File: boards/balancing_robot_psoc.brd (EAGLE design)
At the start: 35 x 75 mm, 19 parts

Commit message: PsoC and MPU board finished
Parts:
- removed C1, C2, C5, C6: 100n, rcl:C0603
- removed C10, C12: 3n3, rcl:C0603
- removed C3, C4, C7, C8: 10u, rcl:153CLV-0405
- removed JP2, JP3: (no value), pinhead:1X06
- removed U$3, U$6: TB6612FNG, SparkFun-PowerIC:SSOP24
- removed U$4: TRANSFORMER, DC_DC_transformer:TRANSFORMER
- removed X1: (no value), con-ptr500:AK500/2
- added LED2, LED3, LED4, LED5, LED6, LED7, LED8: (no value), led:CHIP-LED0603
- added R10, R11, R12, R13, R14, R15, R16, R17, R2, R3, R4, R5, R6, R7, R8, R9: (no value), rcl:R0603
- added U$1: PSOC/PROC, SmartCart:PSOC/PROC_SOCKET
- added U$5: MPU, MPU:MPU
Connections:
- removed net OUT_MOTOR1_1: C12.2, JP2.6, U$6.1, U$6.11, U$6.12, U$6.2
- removed net OUT_MOTOR1_2: C12.1, JP2.5, U$6.5, U$6.6, U$6.7, U$6.8
- removed net OUT_MOTOR2_1: C10.2, JP3.6, U$3.1, U$3.11, U$3.12, U$3.2
- removed net OUT_MOTOR2_2: C10.1, JP3.5, U$3.5, U$3.6, U$3.7, U$3.8
- new net 3V3: JP1.7, JP1.8, R7.2
- new net 5V: JP1.1, JP1.2, R1.2, R6.2, U$5.P$1
- new net ADC_BAT: R8.2, R9.1, U$1.1.16
- new net CONN1: R10.2, R11.2, R12.2, R13.2, R14.2, R15.2, R16.2, R17.1
- new net GPIO_0: JP1.11, U$1.1.7
- new net GPIO_1: JP1.12, U$1.1.9
- new net I2C_SCL: JP1.14, U$1.1.19, U$5.P$3
- new net I2C_SDA: JP1.13, U$1.1.20, U$5.P$4
- new net LED0: LED4.C, U$1.2.19
- new net LED1: LED5.C, U$1.2.20
- new net LED2: LED3.C, U$1.2.17
- new net LED3: LED6.C, U$1.2.18
- new net LED4: LED2.C, U$1.2.15
- new net LED5: LED7.C, U$1.2.16
- new net LED6: LED8.C, U$1.2.14
- new net N$1: R2.2, U$1.1.23
- new net N$11: LED4.A, R12.1
- new net N$12: LED5.A, R13.1
- new net N$13: LED6.A, R14.1
- new net N$14: LED7.A, R15.1
- new net N$15: LED8.A, R16.1
- new net N$2: R5.1, U$1.2.13
- new net N$3: R3.2, U$1.2.2
- new net N$4: R4.1, U$1.1.2
- new net N$5: LED2.A, R10.1
- new net N$6: LED3.A, R11.1
- new net POWER_SUP: R17.2, R2.1, R3.1, R4.2, R5.2, R6.1, R7.1
- new net UART_RX: JP1.10, U$1.2.5
- new net UART_TX: JP1.9, U$1.2.9
- net ENK_MOTOR1A: now also U$1.1.22; no longer JP2.3
- net ENK_MOTOR1B: now also U$1.1.21; no longer JP2.2
- net ENK_MOTOR2A: now also U$1.1.18; no longer JP3.3
- net ENK_MOTOR2B: now also U$1.1.17; no longer JP3.2
- net GND: now also R8.1, U$1.1.1, U$1.1.24, U$1.2.4, U$5.P$2; no longer C1.1, C2.2, C3.-, C4.-, C5.1, C6.2, C7.-, C8.-, JP2.1, JP3.1, U$3.10, U$3.18, U$3.3, U$3.4, U$3.9, U$4.1IN-, U$4.1OUT-, U$4.2IN-, U$4.2OUT-, U$6.10, U$6.18, U$6.3, U$6.4, U$6.9, X1.2
- net MOTOR1_1: now also U$1.2.3; no longer U$6.17, U$6.21
- net MOTOR1_2: now also U$1.2.7; no longer U$6.16, U$6.22
- net MOTOR1_PWM: now also U$1.2.8; no longer U$6.15, U$6.23
- net MOTOR2_1: now also U$1.2.10; no longer U$3.17, U$3.21
- net MOTOR2_2: now also U$1.2.11; no longer U$3.16, U$3.22
- net MOTOR2_PWM: now also U$1.2.12; no longer U$3.15, U$3.23
- net VCC: now also R9.2; no longer C1.2, C2.1, C3.+, C4.+, C5.2, C6.1, C7.+, C8.+, JP1.1, JP1.2, JP2.4, JP3.4, R1.2, U$3.13, U$3.14, U$3.20, U$3.24, U$4.1IN+, U$4.1OUT+, U$4.2IN+, U$4.2OUT+, U$6.13, U$6.14, U$6.20, U$6.24, X1.1
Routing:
- net VCC: track 253.0 -> 5.74 mm, vias 7 -> 0
- net POWER_SUP: track 0.00 -> 121.8 mm, vias 0 -> 2
- net I2C_SCL: track 0.00 -> 60.6 mm
- net I2C_SDA: track 0.00 -> 60.1 mm
- net OUT_MOTOR2_1: track 57.5 -> 0.00 mm, vias 4 -> 0
- net OUT_MOTOR2_2: track 39.4 -> 0.00 mm, vias 2 -> 0
- net 5V: track 0.00 -> 37.9 mm
- net UART_TX: track 0.00 -> 35.8 mm, vias 0 -> 1
- net ADC_BAT: track 0.00 -> 32.0 mm
- net LED4: track 0.00 -> 31.5 mm
- net OUT_MOTOR1_1: track 29.5 -> 0.00 mm, vias 4 -> 0
- net UART_RX: track 0.00 -> 28.8 mm, vias 0 -> 1
- net LED2: track 0.00 -> 26.1 mm
- net CONN1: track 0.00 -> 22.8 mm
- net LED6: track 0.00 -> 21.9 mm
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
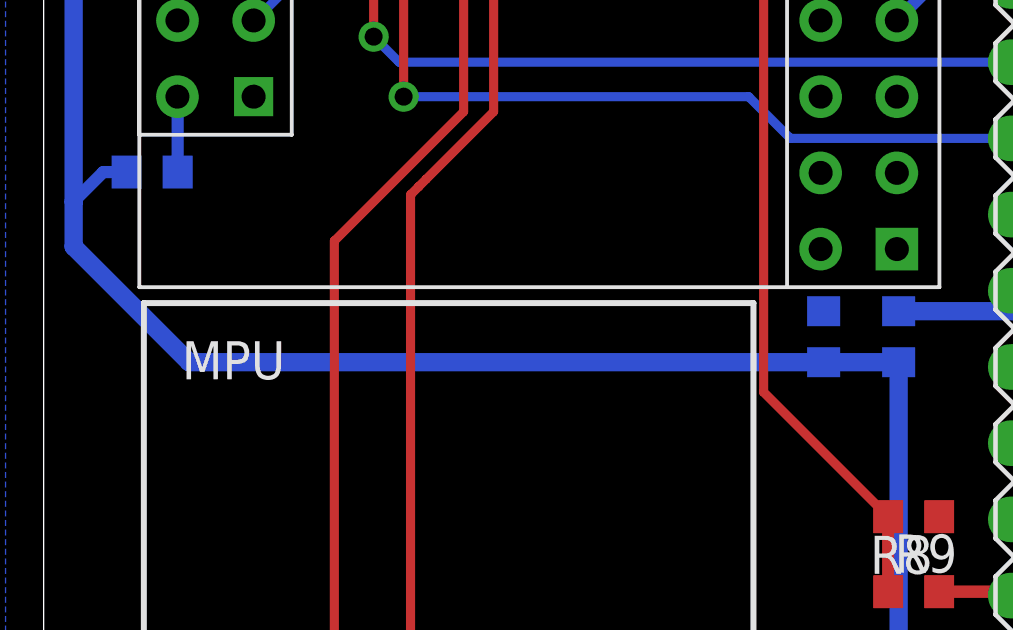
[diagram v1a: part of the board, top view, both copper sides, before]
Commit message: added capacitors on power sup line on psoc board
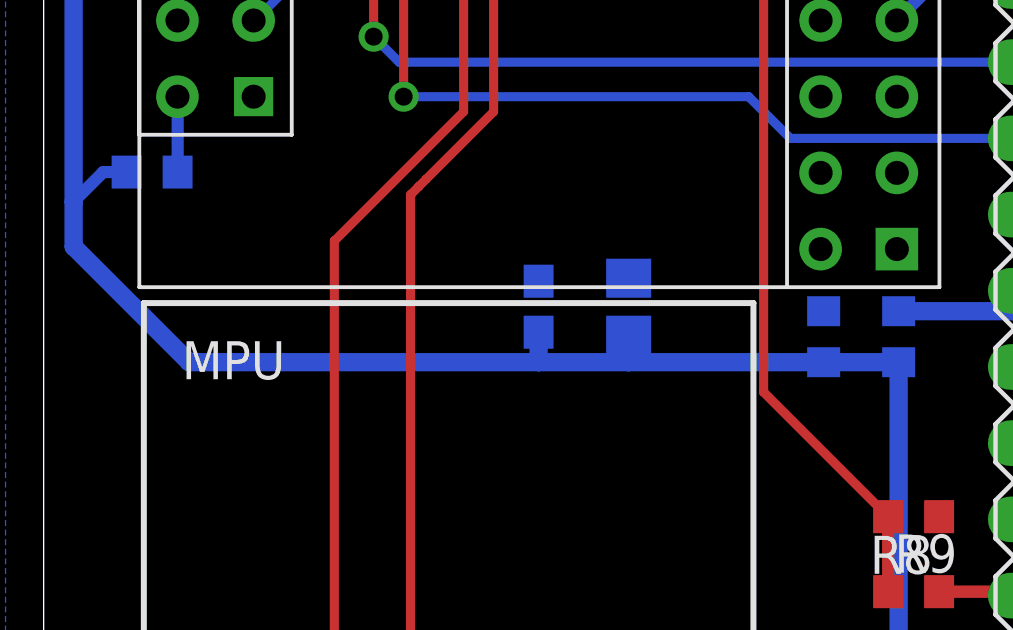
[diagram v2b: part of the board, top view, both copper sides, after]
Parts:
- added C1: (no value), rcl:C0603
- added C2: (no value), rcl:C0805
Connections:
- net GND: now also C1.2, C2.2
- net POWER_SUP: now also C1.1, C2.1
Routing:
- net POWER_SUP: track 121.8 -> 123.7 mm
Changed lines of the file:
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@@
 <layer number="27" name="tValues" color="7" fill="1" visible="yes" active="yes"/>
 <layer number="28" name="bValues" color="7" fill="1" visible="yes" active="yes"/>
-<layer number="29" name="tStop" color="7" fill="3" visible="yes" active="yes"/>
-<layer number="30" name="bStop" color="7" fill="6" visible="yes" active="yes"/>
+<layer number="29" name="tStop" color="7" fill="3" visible="no" active="yes"/>
+<layer number="30" name="bStop" color="7" fill="6" visible="no" active="yes"/>
 <layer number="31" name="tCream" color="7" fill="4" visible="no" active="yes"/>
 <layer number="32" name="bCream" color="7" fill="5" visible="no" active="yes"/>
@@
 <element name="R16" library="rcl" package="R0603" value="" x="7" y="66" rot="R90"/>
 <element name="R17" library="rcl" package="R0603" value="" x="17.5" y="69.5" rot="R90"/>
+<element name="C1" library="rcl" package="C0603" value="" x="16.5" y="23" rot="MR90"/>
+<element name="C2" library="rcl" package="C0805" value="" x="19.5" y="23" rot="MR90"/>
 </elements>
 <signals>
@@
 <via x="10.16" y="50.8" extent="1-16" drill="0.6"/>
 <via x="21.59" y="5.08" extent="1-16" drill="0.6"/>
+<contactref element="C1" pad="2"/>
+<contactref element="C2" pad="2"/>
 </signal>
 <signal name="VCC">
@@
 <wire x1="2.766409375" y1="27.487071875" x2="1.987071875" y2="27.487071875" width="0.4064" layer="16"/>
 <wire x1="1.987071875" y1="27.487071875" x2="1" y2="26.5" width="0.4064" layer="16"/>
-<wire x1="4.85" y1="21.15" x2="26" y2="21.15" width="0.6096" layer="16"/>
+<wire x1="4.85" y1="21.15" x2="16.5" y2="21.15" width="0.6096" layer="16"/>
+<wire x1="16.5" y1="21.15" x2="19.5" y2="21.15" width="0.6096" layer="16"/>
+<wire x1="19.5" y1="21.15" x2="26" y2="21.15" width="0.6096" layer="16"/>
 <wire x1="26" y1="21.15" x2="28.5" y2="21.15" width="0.6096" layer="16"/>
 <wire x1="21.65" y1="57" x2="11.5" y2="57" width="0.4064" layer="1"/>
@@
 <via x="17.5" y="71.5" extent="1-16" drill="0.6"/>
 <wire x1="17.5" y1="71.5" x2="17.5" y2="70.35" width="0.6096" layer="1"/>
+<contactref element="C1" pad="1"/>
+<contactref element="C2" pad="1"/>
+<wire x1="16.5" y1="22.15" x2="16.5" y2="21.15" width="0.6096" layer="16"/>
+<wire x1="19.5" y1="22.05" x2="19.5" y2="21.15" width="0.6096" layer="16"/>
 </signal>
 <signal name="3V3">

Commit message: final changes of boards - production version
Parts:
- added C3: (no value), rcl:C0603
- moved R17 0.50 mm to (17.5, 69.0)
- moved R2 0.50 mm to (22.5, 56.5)
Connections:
- net GND: now also C3.2
- net N$2: now also C3.1
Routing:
- net N$2: track 5.02 -> 7.68 mm
- net POWER_SUP: track 123.7 -> 124.2 mm
- net N$1: track 8.44 -> 7.94 mm
- net CONN1: track 22.8 -> 22.3 mm

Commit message: satland production version of boards
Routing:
- net N$4: track 0.00 -> 2.17 mm
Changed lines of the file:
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@@
 <param name="mdSmdStop" value="0mil"/>
 <param name="msWidth" value="10mil"/>
-<param name="msDrill" value="24mil"/>
+<param name="msDrill" value="0.05mm"/>
 <param name="msMicroVia" value="9.99mm"/>
 <param name="msBlindViaRatio" value="0.5"/>
@@
 <contactref element="U$1" pad="1.2"/>
 <contactref element="R4" pad="1"/>
-<wire x1="26" y1="22.85" x2="25.9" y2="24.92" width="0" layer="19" extent="16-16"/>
+<wire x1="26" y1="22.85" x2="25.9" y2="22.85" width="0.6096" layer="16"/>
+<wire x1="25.9" y1="22.85" x2="25.9" y2="24.92" width="0.6096" layer="16"/>
 </signal>
 <signal name="POWER_SUP">
